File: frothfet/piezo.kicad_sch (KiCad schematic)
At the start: 3 parts, among them J14 FAN, Q10 AO3400A

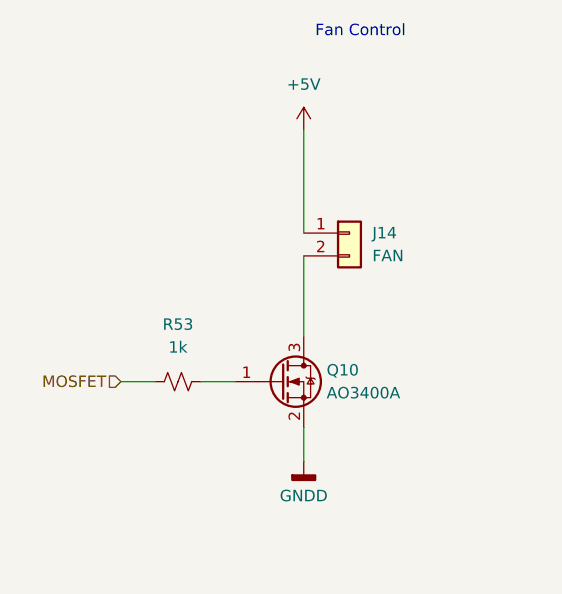
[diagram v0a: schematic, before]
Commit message: added piezo buzzer
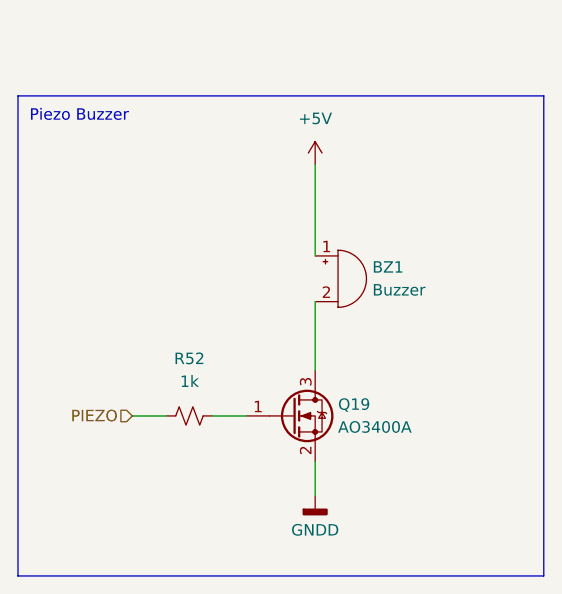
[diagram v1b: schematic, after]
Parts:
- removed J14: FAN, Connector_JST:JST_PH_B2B-PH-SM4-TB_1x02-1MP_P2.00mm_Vertical, symbol Connector_Generic:Conn_01x02
- removed Q10: AO3400A, Package_TO_SOT_SMD:SOT-23, symbol Transistor_FET:AO3400A
- removed R53: 1k, Resistor_SMD:R_0805_2012Metric_Pad1.20x1.40mm_HandSolder, symbol Device:R_Small_US
- added BZ1: Buzzer, yarrboard:Buzzer_FUET_9.6x9.6, symbol Device:Buzzer
- added Q19: AO3400A, Package_TO_SOT_SMD:SOT-23, symbol Transistor_FET:AO3400A
- added R52: 1k, Resistor_SMD:R_0805_2012Metric_Pad1.20x1.40mm_HandSolder, symbol Device:R_Small_US
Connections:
- net +5V: now also BZ1.1 (+)
- net GNDD: now also Q19.2 (S)
- new net: Q19.1 (G), R52.1
- new net: BZ1.2 (-), Q19.3 (D)
- new net PIEZO: R52.2
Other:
- note added: "Piezo Buzzer"
- note removed: "Fan Control"

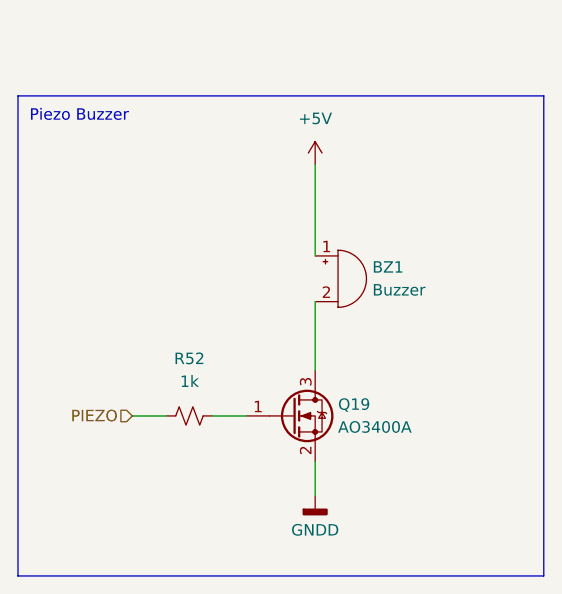
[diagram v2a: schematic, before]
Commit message: updated the dummy load schematic.
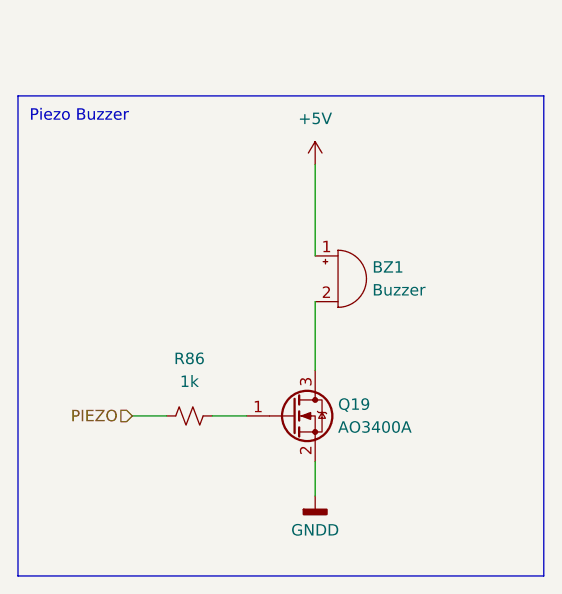
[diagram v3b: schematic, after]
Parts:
- renumbered R52 to R86
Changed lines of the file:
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@@
 		(dnp no)
 		(fields_autoplaced yes)
-		(property "Reference" "R52"
+		(property "Reference" "R86"
 			(at 120.65 93.98 90)
 			(effects
@@
 			(project "frothfet"
 				(path "/c83c6236-96e9-46ad-9d7a-9e2efa4a7966/13bd1484-e1d0-414c-b70b-256f3904dbbc"
-					(reference "R52")
+					(reference "R86")
 					(unit 1)
 				)
@@
 		(dnp no)
 		(fields_autoplaced yes)
-		(property "Reference" "#PWR058"
+		(property "Reference" "#PWR0113"
 			(at 134.62 76.2 0)
 			(effects
@@
 			(project "frothfet"
 				(path "/c83c6236-96e9-46ad-9d7a-9e2efa4a7966/13bd1484-e1d0-414c-b70b-256f3904dbbc"
-					(reference "#PWR058")
+					(reference "#PWR0113")
 					(unit 1)
 				)
@@
 		(dnp no)
 		(fields_autoplaced yes)
-		(property "Reference" "#PWR061"
+		(property "Reference" "#PWR0114"
 			(at 134.62 115.57 0)
 			(effects
@@
 			(project "frothfet"
 				(path "/c83c6236-96e9-46ad-9d7a-9e2efa4a7966/13bd1484-e1d0-414c-b70b-256f3904dbbc"
-					(reference "#PWR061")
-					(unit 1)
-				)
+					(reference "#PWR0114")
+					(unit 1)
+				)

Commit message: started work on rev e, looking clean at 13mm
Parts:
- renumbered R86 to R98
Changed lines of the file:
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@@
 		(dnp no)
 		(fields_autoplaced yes)
-		(property "Reference" "R86"
+		(property "Reference" "R98"
 			(at 120.65 93.98 90)
 			(effects
@@
 			(project "frothfet"
 				(path "/c83c6236-96e9-46ad-9d7a-9e2efa4a7966/13bd1484-e1d0-414c-b70b-256f3904dbbc"
-					(reference "R86")
+					(reference "R98")
 					(unit 1)
 				)
@@
 		(dnp no)
 		(fields_autoplaced yes)
-		(property "Reference" "#PWR0113"
+		(property "Reference" "#PWR0115"
 			(at 134.62 76.2 0)
 			(effects
@@
 			(project "frothfet"
 				(path "/c83c6236-96e9-46ad-9d7a-9e2efa4a7966/13bd1484-e1d0-414c-b70b-256f3904dbbc"
-					(reference "#PWR0113")
+					(reference "#PWR0115")
 					(unit 1)
 				)
@@
 		(dnp no)
 		(fields_autoplaced yes)
-		(property "Reference" "#PWR0114"
+		(property "Reference" "#PWR0116"
 			(at 134.62 115.57 0)
 			(effects
@@
 			(project "frothfet"
 				(path "/c83c6236-96e9-46ad-9d7a-9e2efa4a7966/13bd1484-e1d0-414c-b70b-256f3904dbbc"
-					(reference "#PWR0114")
-					(unit 1)
-				)
+					(reference "#PWR0116")
+					(unit 1)
+				)

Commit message: changed to 0603 and various tweaks
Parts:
- R98: footprint Resistor_SMD:R_0805_2012Metric_Pad1.20x1.40mm_HandSolder -> Resistor_SMD:R_0603_1608Metric
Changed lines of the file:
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@@
 			)
 		)
-		(property "Footprint" "Resistor_SMD:R_0805_2012Metric_Pad1.20x1.40mm_HandSolder"
+		(property "Footprint" "Resistor_SMD:R_0603_1608Metric"
 			(at 120.65 100.33 0)
 			(effects

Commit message: updated to kicad v9
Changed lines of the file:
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@@
 (kicad_sch
-	(version 20231120)
+	(version 20250114)
 	(generator "eeschema")
-	(generator_version "8.0")
+	(generator_version "9.0")
 	(paper "A4")
 	(title_block
@@
 		(rev "E")
 		(company "https://github.com/hoeken/frothfet")
+	)
+	(rectangle
+		(start 101.6 64.77)
+		(end 160.02 118.11)
+		(stroke
+			(width 0)
+			(type default)
+		)
+		(fill
+			(type none)
+		)
+	)
+	(text "Piezo Buzzer"
+		(exclude_from_sim no)
+		(at 102.87 67.818 0)
+		(effects
+			(font
+				(size 1.27 1.27)
+			)
+			(justify left bottom)
+		)
 	)
 	(wire
@@
 		)
 	)
-	(rectangle
-		(start 101.6 64.77)
-		(end 160.02 118.11)
-		(stroke
-			(width 0)
-			(type default)
-		)
-		(fill
-			(type none)
-		)
-	)
-	(text "Piezo Buzzer"
-		(exclude_from_sim no)
-		(at 102.87 67.818 0)
-		(effects
-			(font
-				(size 1.27 1.27)
-			)
-			(justify left bottom)
-		)
-	)
 	(hierarchical_label "PIEZO"
 		(shape input)
 		(at 114.3 100.33 180)
-		(fields_autoplaced yes)
 		(effects
 			(font

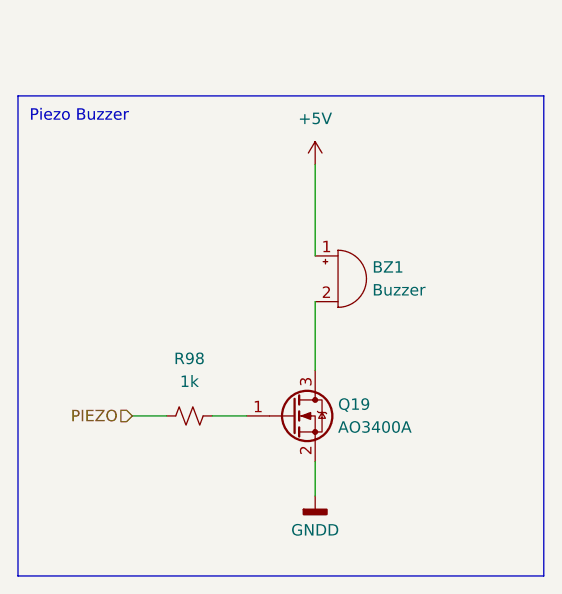
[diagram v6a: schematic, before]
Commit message: worked on the bom and footprint placement
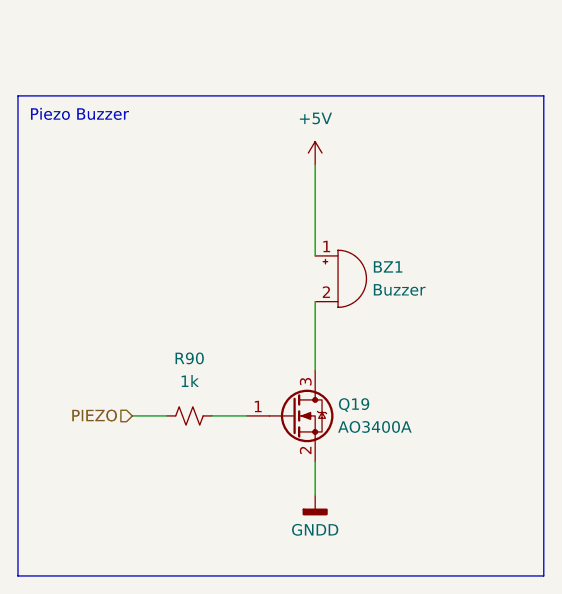
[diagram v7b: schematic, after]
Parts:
- R90: renamed from R98; LCSC C95781 -> (none)
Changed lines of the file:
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@@
 		(dnp no)
 		(fields_autoplaced yes)
-		(property "Reference" "R98"
+		(property "Reference" "R90"
 			(at 120.65 93.98 90)
 			(effects
@@
 			)
 		)
-		(property "LCSC" "C95781"
+		(property "LCSC" ""
 			(at 120.65 100.33 0)
 			(effects
@@
 			(project "frothfet"
 				(path "/c83c6236-96e9-46ad-9d7a-9e2efa4a7966/13bd1484-e1d0-414c-b70b-256f3904dbbc"
-					(reference "R98")
+					(reference "R90")
 					(unit 1)
 				)
@@
 		(dnp no)
 		(fields_autoplaced yes)
-		(property "Reference" "#PWR0115"
+		(property "Reference" "#PWR0108"
 			(at 134.62 76.2 0)
 			(effects
@@
 			(project "frothfet"
 				(path "/c83c6236-96e9-46ad-9d7a-9e2efa4a7966/13bd1484-e1d0-414c-b70b-256f3904dbbc"
-					(reference "#PWR0115")
+					(reference "#PWR0108")
 					(unit 1)
 				)
@@
 		(dnp no)
 		(fields_autoplaced yes)
-		(property "Reference" "#PWR0116"
+		(property "Reference" "#PWR0109"
 			(at 134.62 115.57 0)
 			(effects
@@
 			(project "frothfet"
 				(path "/c83c6236-96e9-46ad-9d7a-9e2efa4a7966/13bd1484-e1d0-414c-b70b-256f3904dbbc"
-					(reference "#PWR0116")
-					(unit 1)
-				)
+					(reference "#PWR0109")
+					(unit 1)
+				)
